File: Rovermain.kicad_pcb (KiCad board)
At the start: 2 copper layers, 120 x 105 mm, 63 parts, among them J1 48V input, J10 3V3 Output, J11 5V Output, J12 Pi_48V_Control, J13 Steering Bus Bar, J14 Drive Bus Bar, J15 Arm Bus Bar, J17 Spare 48V port, J2 USB_C_Receptacle_Pi_Power, J3 24V Output, J4 USB_C_Receptacle_Spare_power, J5 Buck 48/24, J6 Buck 24/12, J7 Buck 24/5, J8 Buck 12/3V3, J9 12V Output, Q1 Arm ctrl, Q2 Steer ctrl, Q3 Drive ctrl, Q4 Spare ctrl, SW2 SW_Push_Open

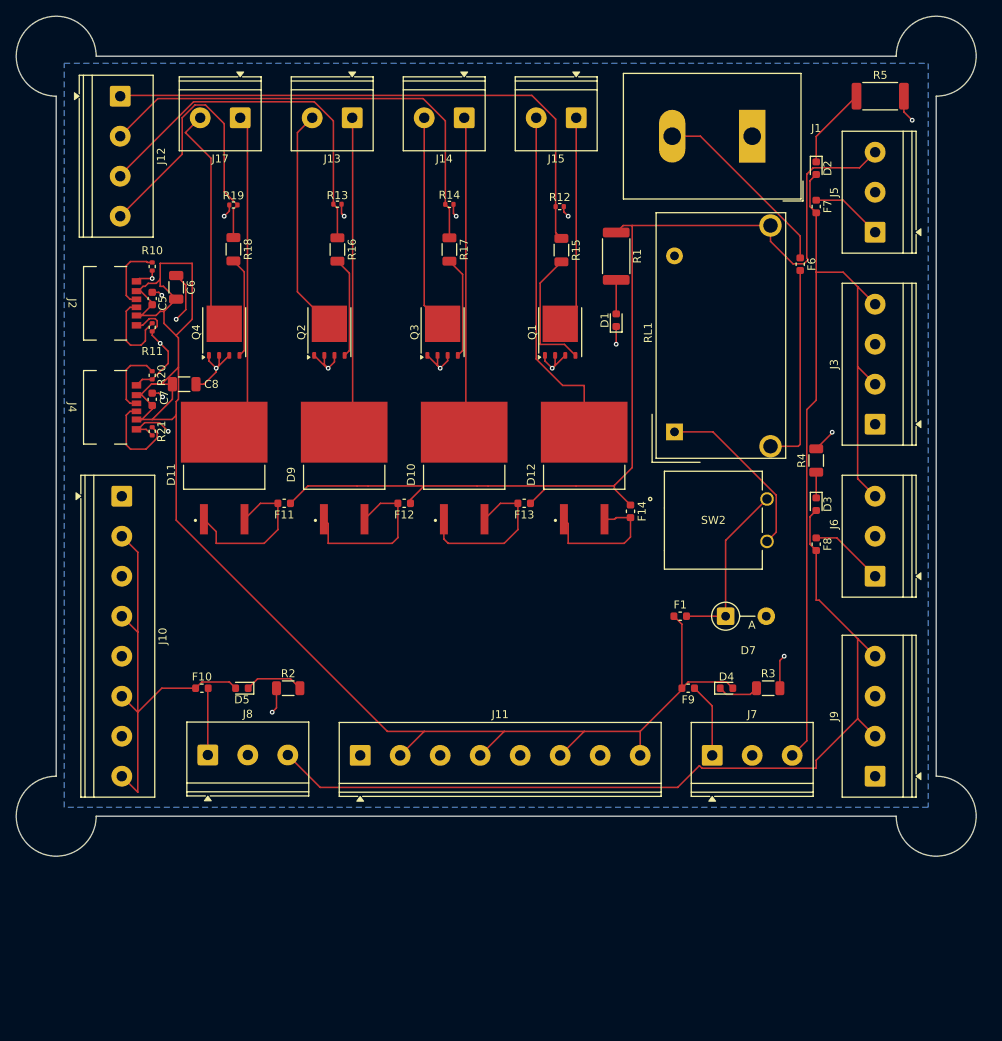
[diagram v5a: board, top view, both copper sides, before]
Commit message: removed high amperage lines, populated 3D model, added mounting
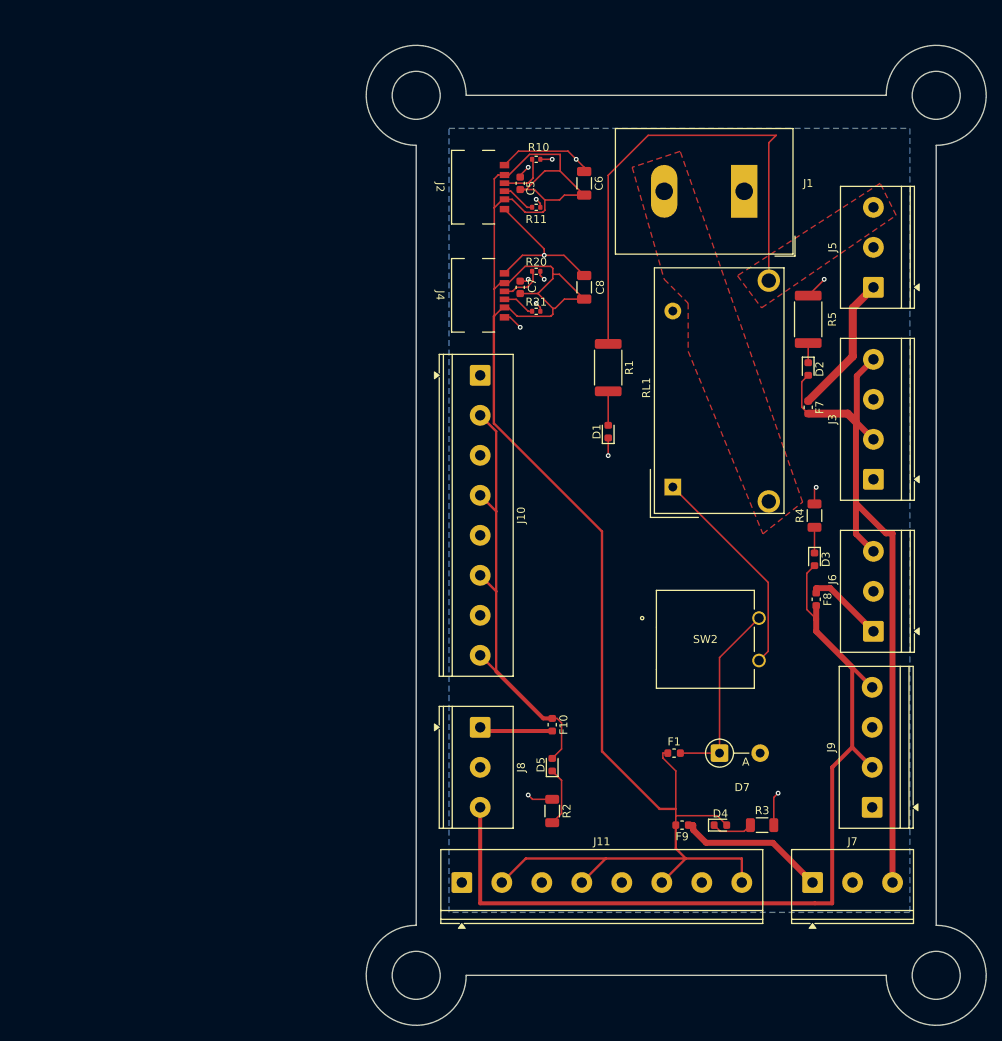
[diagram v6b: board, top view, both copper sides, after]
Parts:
- removed D10, D11, D12, D9: D, SM74611KTTR:TO254P1524X483-3N
- removed F11, F12, F13, F14, F6: Fuse, Fuse:Fuse_0603_1608Metric
- removed J12: Pi_48V_Control, TerminalBlock_Phoenix:TerminalBlock_Phoenix_PT-1,5-4-5.0-H_1x04_P5.00mm_Horizontal
- removed J13: Steering Bus Bar, TerminalBlock_Phoenix:TerminalBlock_Phoenix_PT-1,5-2-5.0-H_1x02_P5.00mm_Horizontal
- removed J14: Drive Bus Bar, TerminalBlock_Phoenix:TerminalBlock_Phoenix_PT-1,5-2-5.0-H_1x02_P5.00mm_Horizontal
- removed J15: Arm Bus Bar, TerminalBlock_Phoenix:TerminalBlock_Phoenix_PT-1,5-2-5.0-H_1x02_P5.00mm_Horizontal
- removed J17: Spare 48V port, TerminalBlock_Phoenix:TerminalBlock_Phoenix_PT-1,5-2-5.0-H_1x02_P5.00mm_Horizontal
- removed Q1: Arm ctrl, Package_TO_SOT_SMD:TDSON-8-1
- removed Q2: Steer ctrl, Package_TO_SOT_SMD:TDSON-8-1
- removed Q3: Drive ctrl, Package_TO_SOT_SMD:TDSON-8-1
- removed Q4: Spare ctrl, Package_TO_SOT_SMD:TDSON-8-1
- removed R12, R13, R14, R19: 100kohm, Resistor_SMD:R_0402_1005Metric
- removed R15, R16, R17, R18: 100ohm, Resistor_SMD:R_1206_3216Metric
- added REF**: MountingHole_6mm, MountingHole:MountingHole_6mm, F.Cu at (160.0, 24.0)
- added REF**: MountingHole_6mm, MountingHole:MountingHole_6mm, F.Cu at (225.0, 134.0)
- added REF**: MountingHole_6mm, MountingHole:MountingHole_6mm, F.Cu at (160.0, 134.0)
- added REF**: MountingHole_6mm, MountingHole:MountingHole_6mm, F.Cu at (225.0, 24.0)
- moved C6 52.6 mm to (181.0, 35.0)
- moved C8 51.4 mm to (181.0, 48.0), turned to -90 degrees
- moved R11 50.3 mm to (175.0, 38.0), turned to 0 degrees
- moved R21 50.3 mm to (175.0, 51.0), turned to 0 degrees
- moved R10 49.8 mm to (175.0, 32.0), turned to 0 degrees
- moved R20 49.7 mm to (175.0, 46.0), turned to 0 degrees
- moved J2 48.2 mm to (168.0, 35.5)
- moved C5 48.2 mm to (173.0, 35.0)
- moved C7 48.1 mm to (173.0, 48.0)
- moved J4 48.1 mm to (168.0, 49.0)
- moved J10 47.3 mm to (168.0, 59.0)
- moved F10 44.0 mm to (177.0, 102.7), turned to -90 degrees
- moved D5 39.9 mm to (177.0, 107.7), turned to 90 degrees
- moved R2 36.4 mm to (177.0, 113.5), turned to -90 degrees
- moved J8 34.2 mm to (168.0, 103.0), turned to -90 degrees
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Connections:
- RL1 pad 14: Net-(F6-Pad2) -> Net-(J1-Pin_2)
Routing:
- net Net-(J12-Pin_1): track 70.9 -> 0.00 mm
- net /48V: track 132.0 -> 62.7 mm
- net Net-(J12-Pin_2): track 58.6 -> 0.00 mm
- net Net-(J12-Pin_3): track 46.4 -> 0.00 mm
- net Net-(D12-A): track 45.0 -> 0.00 mm
- net Net-(D11-A): track 40.9 -> 0.00 mm
- net Net-(D9-A): track 39.8 -> 0.00 mm
- net Net-(D10-A): track 39.5 -> 0.00 mm
- net Net-(J12-Pin_4): track 37.5 -> 0.00 mm
- net /+5V: track 195.5 -> 229.4 mm
- net Net-(J15-Pin_1): track 31.3 -> 0.00 mm
- net Net-(J17-Pin_2): track 28.5 -> 0.00 mm
- net Net-(J13-Pin_2): track 28.2 -> 0.00 mm
- net GNDREF: track 84.2 -> 56.8 mm, vias 19 -> 14
- net Net-(J14-Pin_2): track 26.7 -> 0.00 mm
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- added copper zone on F.Cu, net /48V
- added copper zone on F.Cu, net Net-(J1-Pin_2)
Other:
- board size 120 x 105 mm -> 77.5 x 122.5 mm

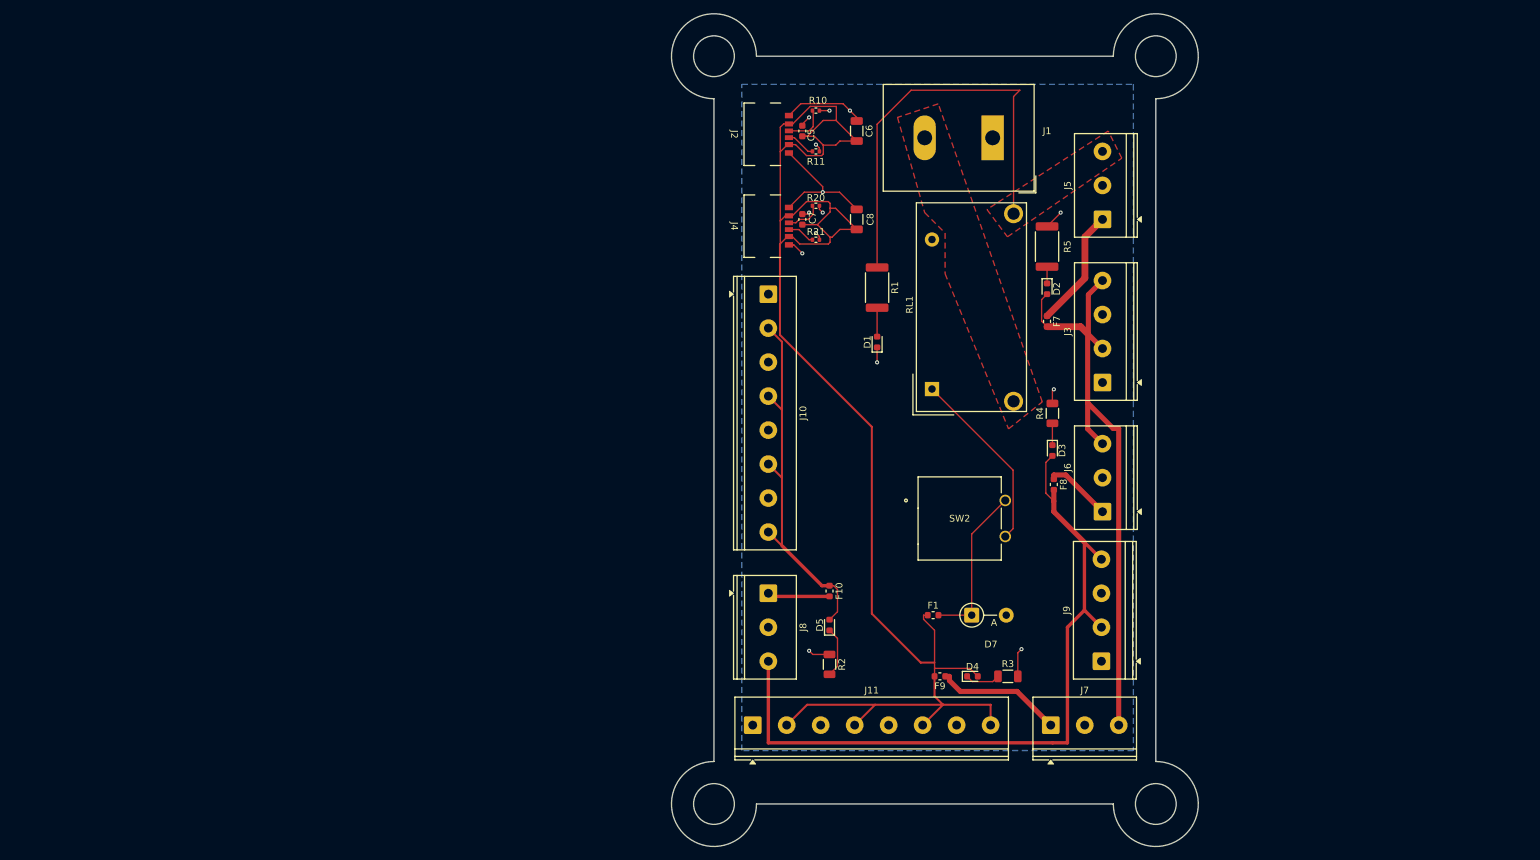
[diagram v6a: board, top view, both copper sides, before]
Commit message: added CAN support; labels
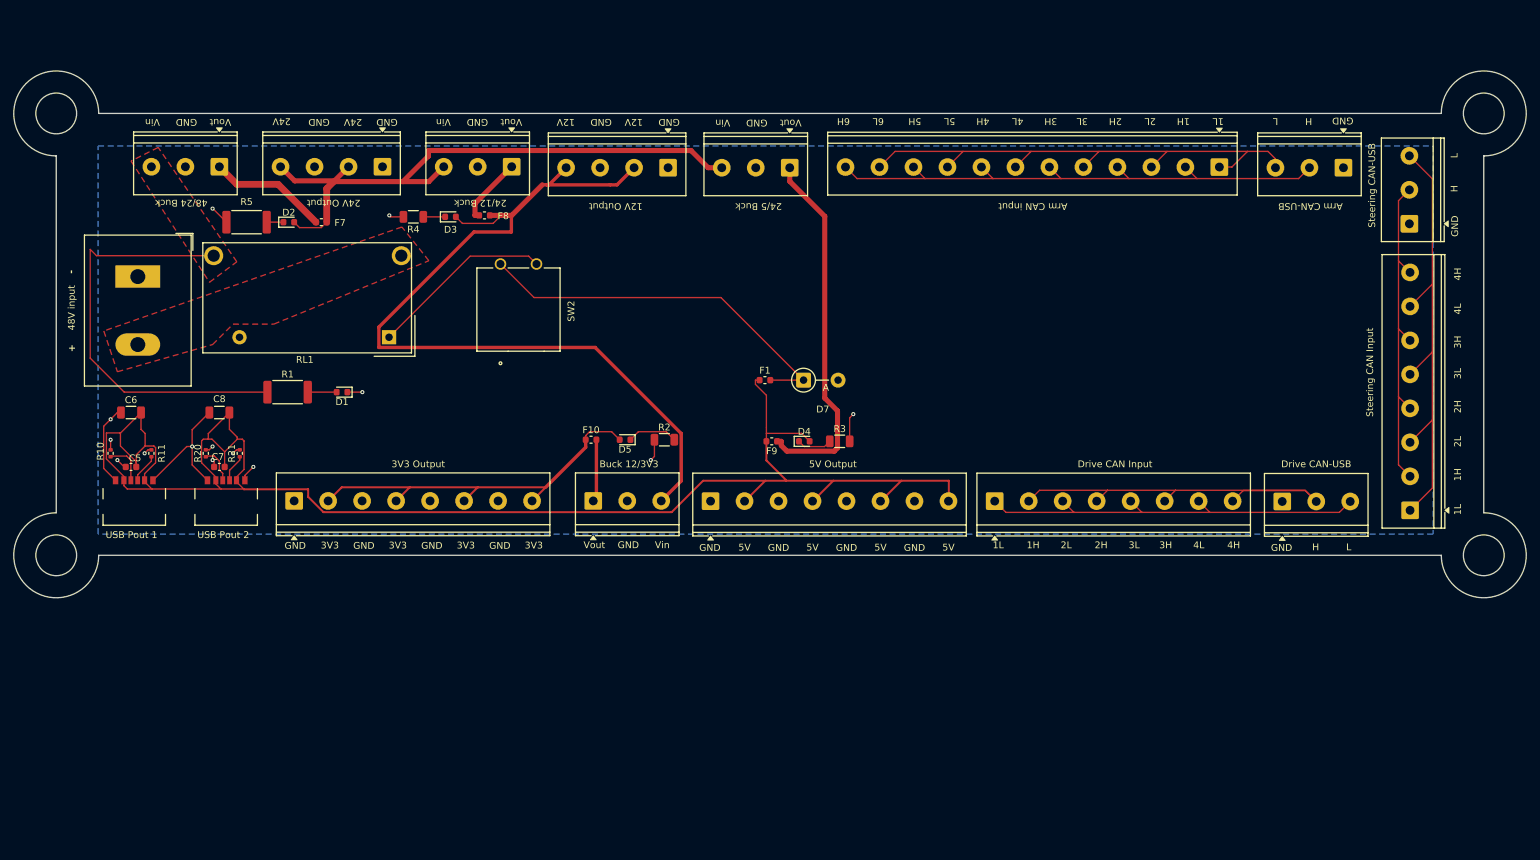
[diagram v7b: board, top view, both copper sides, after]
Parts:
- added J12: Arm CAN-USB, TerminalBlock_Phoenix:TerminalBlock_Phoenix_PT-1,5-3-5.0-H_1x03_P5.00mm_Horizontal, F.Cu at (252.6, 40.4)
- added J13: Drive CAN-USB, TerminalBlock_Phoenix:TerminalBlock_Phoenix_PT-1,5-3-5.0-H_1x03_P5.00mm_Horizontal, F.Cu at (243.6, 89.5)
- added J14: Steering CAN-USB, TerminalBlock_Phoenix:TerminalBlock_Phoenix_PT-1,5-3-5.0-H_1x03_P5.00mm_Horizontal, F.Cu at (262.3, 48.6)
- added J15: Drive CAN Input, TerminalBlock_Phoenix:TerminalBlock_Phoenix_PT-1,5-8-5.0-H_1x08_P5.00mm_Horizontal, F.Cu at (201.3, 89.5)
- added J16: Steering CAN Input, TerminalBlock_Phoenix:TerminalBlock_Phoenix_PT-1,5-8-5.0-H_1x08_P5.00mm_Horizontal, F.Cu at (262.4, 90.8)
- added J17: Arm CAN Input, TerminalBlock_Phoenix:TerminalBlock_Phoenix_PT-1,5-12-5.0-H_1x12_P5.00mm_Horizontal, F.Cu at (234.3, 40.3)
- moved REF** 162.0 mm to (63.2, 32.4), turned to 90 degrees
- moved J5 130.1 mm to (87.2, 40.3), turned to 180 degrees
- moved J1 127.4 mm to (75.2, 56.4), turned to -90 degrees
- moved REF** 121.5 mm to (63.2, 97.4), turned to 90 degrees
- moved REF** 119.0 mm to (273.2, 97.4), turned to 90 degrees
- moved R5 117.8 mm to (91.2, 48.4), turned to 180 degrees
- moved R10 115.4 mm to (71.2, 82.4), turned to 90 degrees
- moved C6 114.5 mm to (74.2, 76.4), turned to 0 degrees
- moved REF** 112.5 mm to (273.2, 32.4), turned to 90 degrees
- moved D2 112.0 mm to (97.5, 48.4), turned to 0 degrees
- moved J3 110.6 mm to (111.2, 40.3), turned to 180 degrees
- moved C5 110.4 mm to (74.2, 84.4), turned to 180 degrees
- moved F7 107.7 mm to (102.2, 48.4), turned to 0 degrees
- moved J2 107.7 mm to (74.7, 89.4), turned to 0 degrees
- moved R11 107.4 mm to (77.2, 82.4), turned to 90 degrees
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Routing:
- net /AH: track 0.00 -> 81.6 mm
- net /AL: track 0.00 -> 79.1 mm
- net /SL: track 0.00 -> 68.9 mm
- net /DH: track 0.00 -> 61.8 mm
- net /DL: track 0.00 -> 60.6 mm
- net /SH: track 0.00 -> 50.7 mm
- net Net-(J7-Pin_1): track 18.8 -> 54.2 mm
- net Net-(D7-K): track 23.8 -> 56.6 mm
- net /12V: track 110.7 -> 127.1 mm
- net /+5V: track 229.4 -> 240.2 mm
- net /24V: track 90.6 -> 91.1 mm
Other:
- board size 77.5 x 122.5 mm -> 222.5 x 77.5 mm
- board text added: "+"
- board text added: "-"
- board text added: "12V"
- board text added: "12V Output"
- board text added: "1H"
- board text added: "1L"
- board text added: "24/12 Buck"
- board text added: "24/5 Buck"
- board text added: "24V"
- board text added: "24V Output"
- board text added: "2H"
- board text added: "2L"
- board text added: "3H"
- board text added: "3L"
- board text added: "3V3"
- board text added: "48/24 Buck"
- board text added: "4H"
- board text added: "4L"
- board text added: "5H"
- board text added: "5L"
- board text added: "5V"
- board text added: "6H"
- board text added: "6L"
- board text added: "Arm CAN input"
- board text added: "Arm CAN-USB"
- board text added: "GND"
- board text added: "H"
- board text added: "L"
- board text added: "USB Pout 1"
- board text added: "USB Pout 2"
- board text added: "Vin"
- board text added: "Vout"

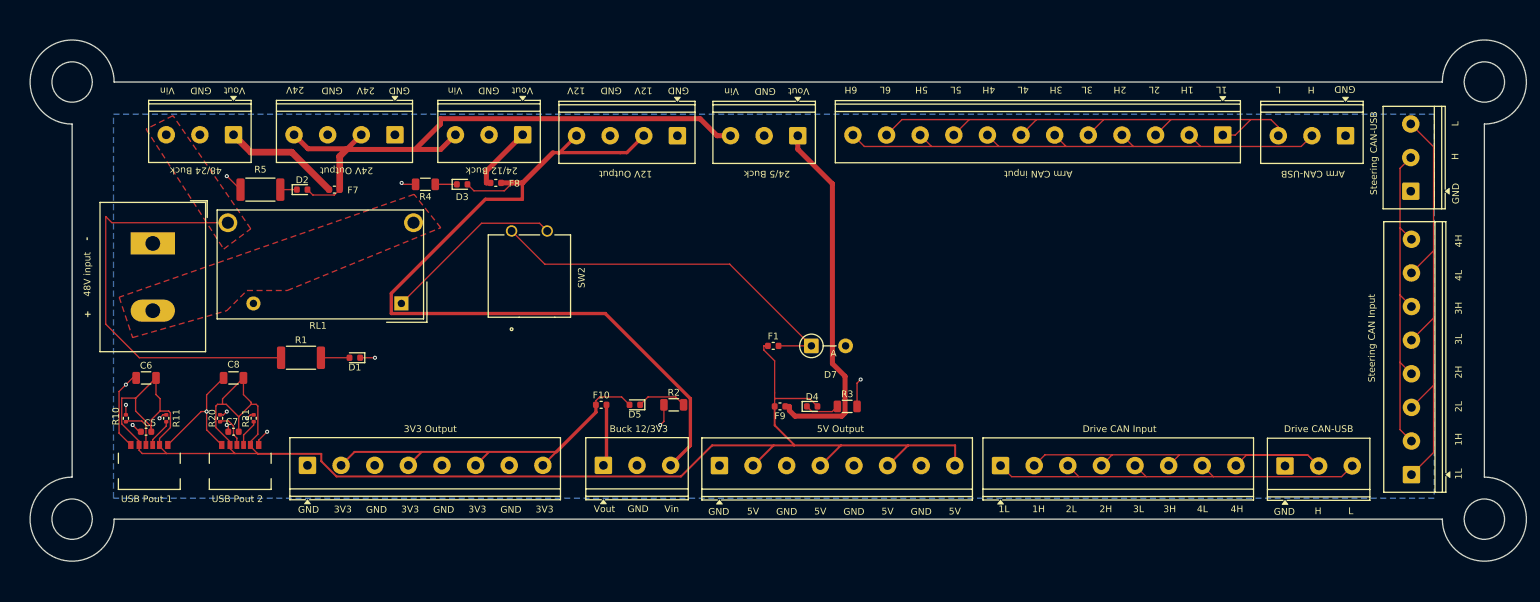
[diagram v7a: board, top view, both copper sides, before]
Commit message: schematic overhaul for CAN2USB
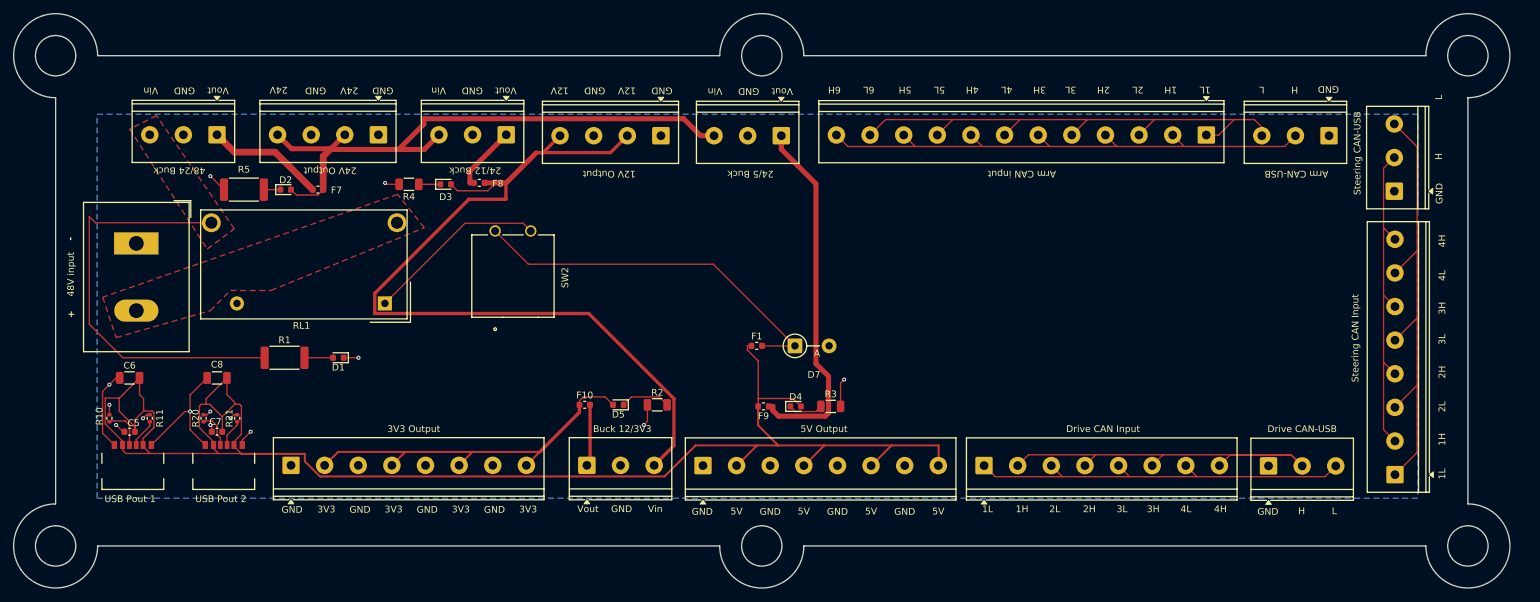
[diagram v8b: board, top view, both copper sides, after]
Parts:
- added REF**: MountingHole_6mm, MountingHole:MountingHole_6mm, F.Cu at (165.8, 28.5)
- added REF**: MountingHole_6mm, MountingHole:MountingHole_6mm, F.Cu at (165.8, 101.4)
- moved REF** 4.68 mm to (270.8, 101.4)
- moved REF** 4.68 mm to (60.8, 101.4)
- moved REF** 4.62 mm to (60.8, 28.5)
- moved REF** 4.62 mm to (270.8, 28.5)
- moved J15 2.45 mm to (198.8, 89.5)
- moved J7 2.45 mm to (168.7, 40.4)
- moved J8 2.45 mm to (139.8, 89.4)
- moved R2 2.45 mm to (150.3, 80.4)
- moved C5 2.45 mm to (71.8, 84.4)
- moved C6 2.45 mm to (71.8, 76.4)
- moved C7 2.45 mm to (84.8, 84.4)
- moved C8 2.45 mm to (84.8, 76.4)
- moved D1 2.45 mm to (102.8, 73.4)
- moved D2 2.45 mm to (95.0, 48.4)
- moved D3 2.45 mm to (118.8, 47.6)
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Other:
- board size 222.5 x 77.5 mm -> 222.5 x 85.4 mm
